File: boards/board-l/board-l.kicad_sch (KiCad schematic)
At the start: 0 parts

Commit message: feat: capture Board L schematic; refactor generator into spec-driven core
Board L: all 68 components (driver, LED array 8x3, logic rail, MCU,
encoder, debug pads) captured from the locked net table in
doc/architecture/board-l.mdx. ERC passes with zero violations and the
exported netlist matches the spec: 45 nets, 178 nodes, 11 intentional
no-connects. Board P regenerated through the same pipeline, still
ERC-clean and netlist-verified.

- scripts/schgen split into schgen_core.py + board_p_spec.py /
  board_l_spec.py + generic gen_schematic.py / verify_netlist.py,
  so the net table lives in exactly one place per board
- symbols lib normalized via kicad-cli sym upgrade (two inductor
  symbols were in legacy KiCad 6 format and tripped
  lib_symbol_mismatch ERC warnings); Conn_1x03 symbol added
- PogoPad_1x03_P2.54mm hand-made UART pad footprint added
- J3 (SWD header) and J4 (UART pads) carry the DNP flag: footprint
  only, excluded from the assembly BOM per the bring-up plan
- LED polarity taken from the symbol drawing: pin 1 = cathode,
  pin 2 = anode; EC11 push-button terminals D/E left no-connect

Co-Authored-By: Claude <noreply@anthropic.com>
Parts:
- added C10, C11, C12, C14: 10uF/50V, zudo-led-lamp:C1206, symbol zudo-led-lamp:CL31A106KBHNNNE
- added C13, C15, C18, C20, C21, C22, C23, C24: 100nF/50V, zudo-led-lamp:C0603, symbol zudo-led-lamp:CC0603KRX7R9BB104
- added C16, C17: 22uF/25V, zudo-led-lamp:C0805, symbol zudo-led-lamp:CL21A226MAQNNNE
- added C19: 1uF/50V, zudo-led-lamp:C0603, symbol zudo-led-lamp:CL10A105KB8NNNC
- added D10: SMAJ20A, zudo-led-lamp:SMA_L4.2-W2.6-LS5.3-RD, symbol zudo-led-lamp:SMAJ20A_C571370
- added D11: SS26, zudo-led-lamp:SMA_L4.3-W2.6-LS5.0-FD, symbol zudo-led-lamp:SS26_C7420363
- added F1: PPTC 750mA/30V, zudo-led-lamp:F1206, symbol zudo-led-lamp:BSMD1206-075-30V
- added J2: B6B-XH-A(LF)(SN), zudo-led-lamp:CONN-TH_6P-P2.50_B6B-XH-A-LF-SN, symbol zudo-led-lamp:B6B-XH-A
- added J3: SWD 1x5 (hand-fit), zudo-led-lamp:HDR-TH_5P-P2.54-V-M, symbol zudo-led-lamp:PZ254V-11-05P
- added J4: UART pads, zudo-led-lamp:PogoPad_1x03_P2.54mm, symbol zudo-led-lamp:Conn_1x03
- added L1: 33uH, zudo-led-lamp:IND-SMD_L7.0-W6.6_FXL0630, symbol zudo-led-lamp:FXL0630-330-M
- added L2: 4.7uH, zudo-led-lamp:IND-SMD_L4.0-W4.0_FNR40XXS, symbol zudo-led-lamp:FNR4030S4R7MT
- added LED1, LED10, LED11, LED12, LED13, LED14, LED15, LED16, LED17, LED18, LED19, LED2, LED20, LED21, LED22, LED23, LED24, LED3, LED4, LED5, LED6, LED7, LED8, LED9: 2835 3000K CRI80, zudo-led-lamp:LED-SMD_L3.3-W2.8-RD, symbol zudo-led-lamp:HL-AM-2835H421W-S1-08-HR3
- added R20, R22, R23, R24, R25, R26: 10k, zudo-led-lamp:R0805, symbol zudo-led-lamp:0805W8F1002T5E
- added R21: 33k, zudo-led-lamp:R0603, symbol zudo-led-lamp:0603WAF3302T5E
- added R30, R31, R32, R33, R34, R35, R36, R37: 33R 1%, zudo-led-lamp:R1206, symbol zudo-led-lamp:FRC1206F33R0TS
- added RS1: 200mR 1% 2W, zudo-led-lamp:R2512, symbol zudo-led-lamp:RLP25FEER200
- added RT1: NTC 10k B3380, zudo-led-lamp:R0603, symbol zudo-led-lamp:NCP18XH103F03RB
- added SW1: EC11 15-detent, zudo-led-lamp:SW-TH_ALPS_EC11L1525G01, symbol zudo-led-lamp:EC11L1525G01
- added U2: AL8860MP-13, zudo-led-lamp:MSOP-8_L3.0-W3.0-P0.65-LS4.9-BL-EP1.8, symbol zudo-led-lamp:AL8860MP-13
- added U3: STM32G031F8P6, zudo-led-lamp:TSSOP-20_L6.5-W4.4-P0.65-LS6.4-BL, symbol zudo-led-lamp:STM32G031F8P6
- added U4: AP63203WU-7, zudo-led-lamp:TSOT-26_L2.9-W1.6-P0.95-LS2.8-BL, symbol zudo-led-lamp:AP63203WU-7
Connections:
- new net ATT: J2.3, R25.2, U3.14 (PA7)
- new net BST: C15.2, U4.6 (BST)
- new net CTRL: C21.1, R20.2, R21.1, U2.4 (CTRL)
- new net ENC_A: C22.1, R22.2, SW1.A, U3.7 (PA0)
- new net ENC_B: C23.1, R23.2, SW1.B, U3.8 (PA1)
- new net GND: C10.2, C11.2, C12.2, C13.2, C14.2, C16.2, C17.2, C18.2, C19.2, C20.2, C21.2, C22.2, C23.2, C24.2, D10.2 (A), J2.5, J2.6, J3.5, J4.3, R21.2, RT1.2, SW1.6 (EH), SW1.7 (EH), SW1.C, U2.2 (GND), U2.3 (GND), U2.9 (EP), U3.5 (VSS/VSSA), U4.4 (GND)
- new net LED_N: D11.1 (A), LED12.1, LED15.1, LED18.1, LED21.1, LED24.1, LED3.1, LED6.1, LED9.1, U2.5 (SW), U2.6 (SW)
- new net LED_P: L1.2, R30.1, R31.1, R32.1, R33.1, R34.1, R35.1, R36.1, R37.1
- new net LED_S1_A: LED1.2, R30.2
- new net LED_S1_M1: LED1.1, LED2.2
- new net LED_S1_M2: LED2.1, LED3.2
- new net LED_S2_A: LED4.2, R31.2
- new net LED_S2_M1: LED4.1, LED5.2
- new net LED_S2_M2: LED5.1, LED6.2
- new net LED_S3_A: LED7.2, R32.2
- new net LED_S3_M1: LED7.1, LED8.2
- new net LED_S3_M2: LED8.1, LED9.2
- new net LED_S4_A: LED10.2, R33.2
- new net LED_S4_M1: LED10.1, LED11.2
- new net LED_S4_M2: LED11.1, LED12.2
- new net LED_S5_A: LED13.2, R34.2
- new net LED_S5_M1: LED13.1, LED14.2
- new net LED_S5_M2: LED14.1, LED15.2
- new net LED_S6_A: LED16.2, R35.2
- new net LED_S6_M1: LED16.1, LED17.2
- new net LED_S6_M2: LED17.1, LED18.2
- new net LED_S7_A: LED19.2, R36.2
- new net LED_S7_M1: LED19.1, LED20.2
- new net LED_S7_M2: LED20.1, LED21.2
- new net LED_S8_A: LED22.2, R37.2
- new net LED_S8_M1: LED22.1, LED23.2
- new net LED_S8_M2: LED23.1, LED24.2
- new net NRST: C20.1, J3.3, U3.6 (PF2-NRST)
- new net NTC_SENSE: C24.1, R26.2, RT1.1, U3.11 (PA4)
- new net PDOK: J2.4, R24.2, U3.12 (PA5)
- new net PWM_DIM: R20.1, U3.13 (PA6)
- new net SET: L1.1, RS1.2, U2.1 (SET)
- new net SWCLK: J3.2, U3.19 (PA15/PA14-BOOT0)
- new net SWDIO: J3.1, U3.18 (PA13)
- new net SW_LOGIC: C15.1, L2.1, U4.5 (SW)
- new net UART_RX: J4.2, U3.10 (PA3)
- new net UART_TX: J4.1, U3.9 (PA2)
- new net V15: C10.1, C11.1, C12.1, C13.1, C14.1, D10.1 (C), D11.2 (K), F1.2, RS1.1, U2.8 (VIN), U4.3 (VIN)
- new net V3P3: C16.1, C17.1, C18.1, C19.1, J3.4, L2.2, R22.1, R23.1, R24.1, R25.1, R26.1, U3.4 (VDD/VDDA), U4.1 (FB)
- new net VBUS_L: F1.1, J2.1, J2.2
- no-connect marks 0 -> 11

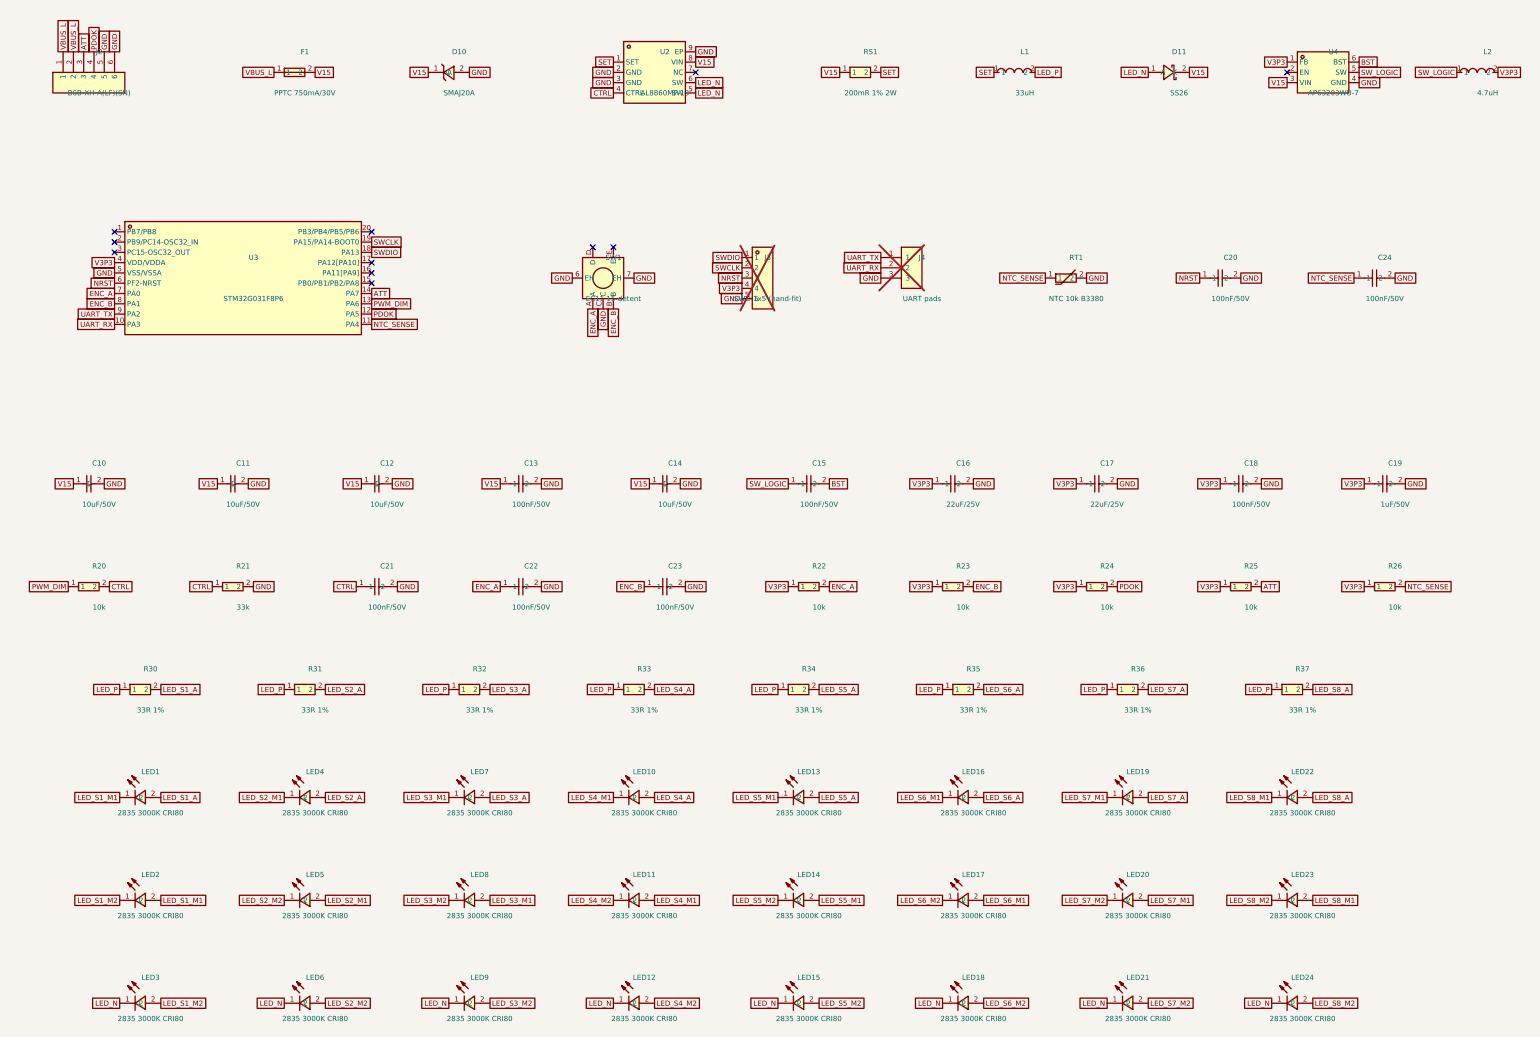
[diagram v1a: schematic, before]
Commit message: fix: schematic readability — labels outside bodies, Board L on A2
- reference/value text now placed from the symbol's pin extents
  (above/below the body) instead of a fixed offset that landed inside
  large IC bodies; per-ref overrides for Q1 and SW1 where vertical
  net labels occupy the default spots
- Board L moved to A2: the 68-part grid collided with the A3 title
  block and bottom border
- connectivity unchanged: both boards still ERC-clean and
  netlist-verified against their specs

Co-Authored-By: Claude <noreply@anthropic.com>
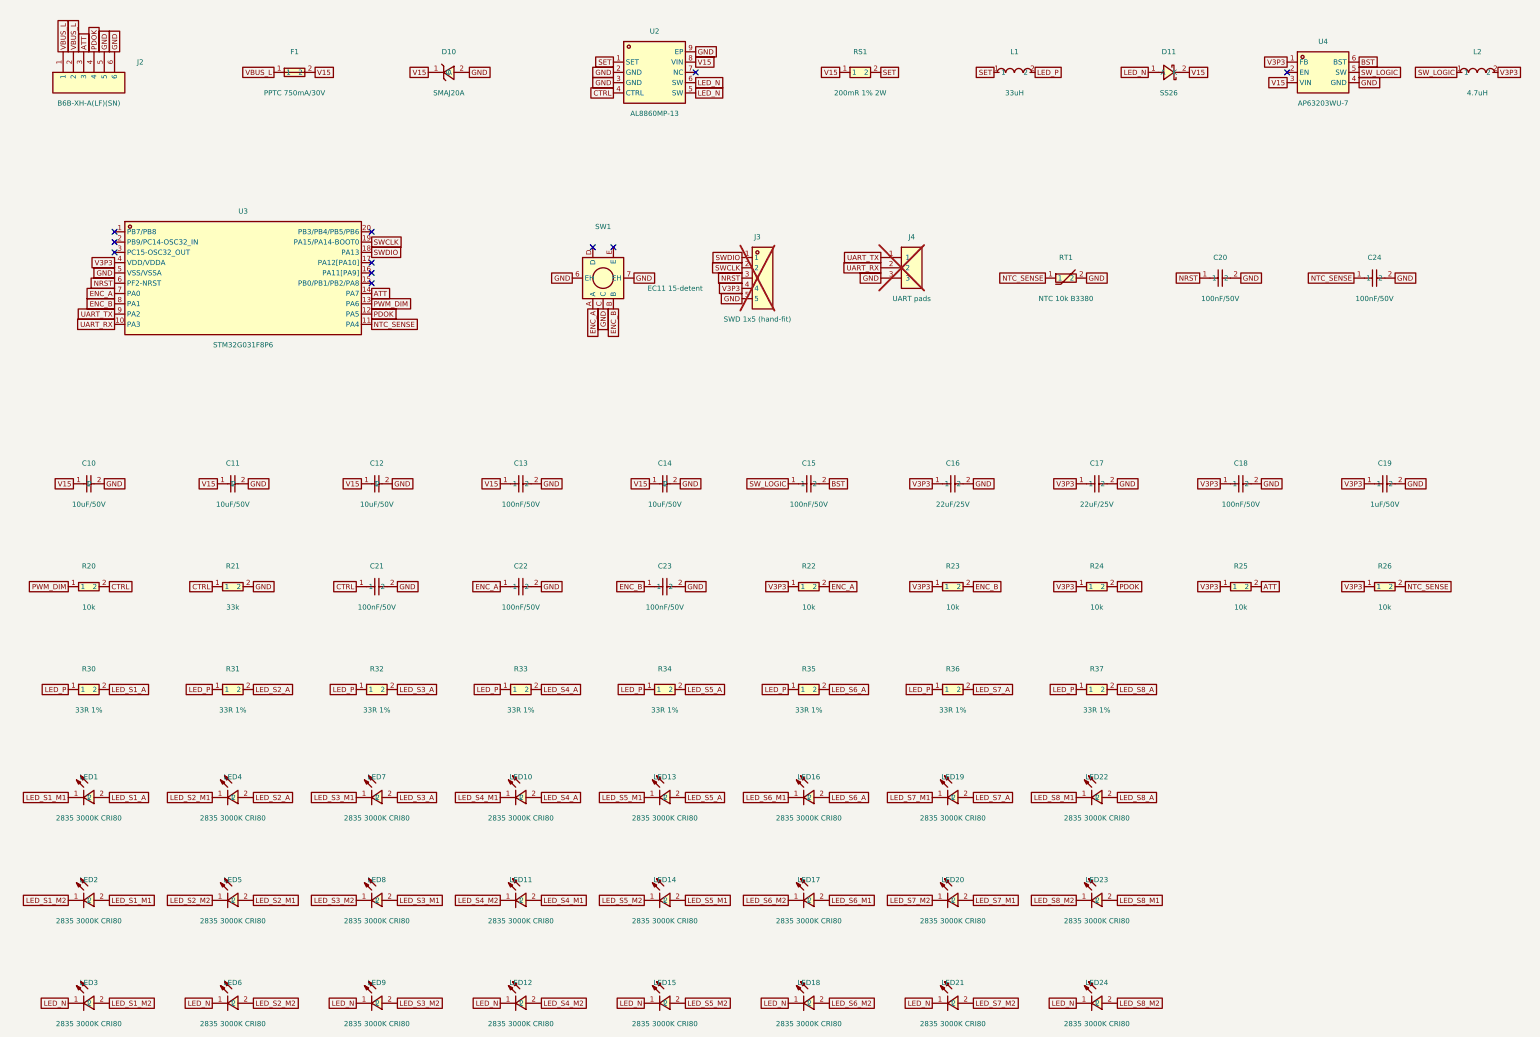
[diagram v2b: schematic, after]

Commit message: fix: apply design-review findings to both boards and docs
Independent electrical review (netlists confirmed pin-for-pin against
datasheets; three real problems found, all fixed before fab):

Board P:
- C35 soft-start re-referenced gate-to-SOURCE (VBUS_IN), not GND.
  Ground-referenced it let Q1 conduct ~16ms at every plug-in and slam
  on un-soft-started at the 5->15V contract step
- R12 56k -> 150k (C22807): old divider put VGS at -12.8V in a 20V
  mis-contract, over the AO3401A's +/-12V abs max; now -8.0V there
- U1.RESET now reaches GND via new R21 10k (C17414) and is brought
  out on J2.4 so the programming jig can recover a wedged NVM write

Board L:
- ballast R30-R37: 1206 250mW -> 2512 1W (C2934070) — the 1206 sat at
  107% of rating at the design's own worst-case 90mA string
- R27/R28 100R (C22775) in series with the encoder phases (contact
  protection for the C22/C23 debounce discharge)
- TP1 bare test pad on CTRL (Gates 3/4 both probe this node)

Docs updated to match: net tables, ratings, BOM (18 Extended lines now,
was 19), duty-cycle figures corrected to datasheet equations (~77%),
LED_P documented as a switching node with layout rules, pulse-skip
dimming-floor check added to Gate 4, R14/R21 open questions resolved
from primary datasheets. Both boards remain ERC-clean and
netlist-verified; doc site builds.

Co-Authored-By: Claude <noreply@anthropic.com>
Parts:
- removed R30, R31, R32, R33, R34, R35, R36, R37: 33R 1%, zudo-led-lamp:R1206, symbol zudo-led-lamp:FRC1206F33R0TS
- added R27, R28: 100R, zudo-led-lamp:R0603, symbol zudo-led-lamp:0603WAF1000T5E
- added R30, R31, R32, R33, R34, R35, R36, R37: 33R 1% 1W, zudo-led-lamp:R2512, symbol zudo-led-lamp:FRC2512F33R0TS
- added TP1: CTRL test pad, zudo-led-lamp:TestPad_D1.5mm, symbol zudo-led-lamp:TestPad
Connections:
- net CTRL: now also TP1.1
- net ENC_A: now also R27.2; no longer SW1.A
- net ENC_B: now also R28.2; no longer SW1.B
- net LED_P: now also R30.1, R31.1, R32.1, R33.1, R34.1, R35.1, R36.1, R37.1
- net LED_S1_A: now also R30.2
- net LED_S2_A: now also R31.2
- net LED_S3_A: now also R32.2
- net LED_S4_A: now also R33.2
- net LED_S5_A: now also R34.2
- net LED_S6_A: now also R35.2
- net LED_S7_A: now also R36.2
- net LED_S8_A: now also R37.2
- new net ENC_A_SW: R27.1, SW1.A
- new net ENC_B_SW: R28.1, SW1.B
